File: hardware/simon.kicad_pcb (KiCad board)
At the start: 2 copper layers, 19 parts, among them SW0 SW_RED, SW1 SW_YELLOW, SW2 SW_GREEN, SW3 SW_BLUE

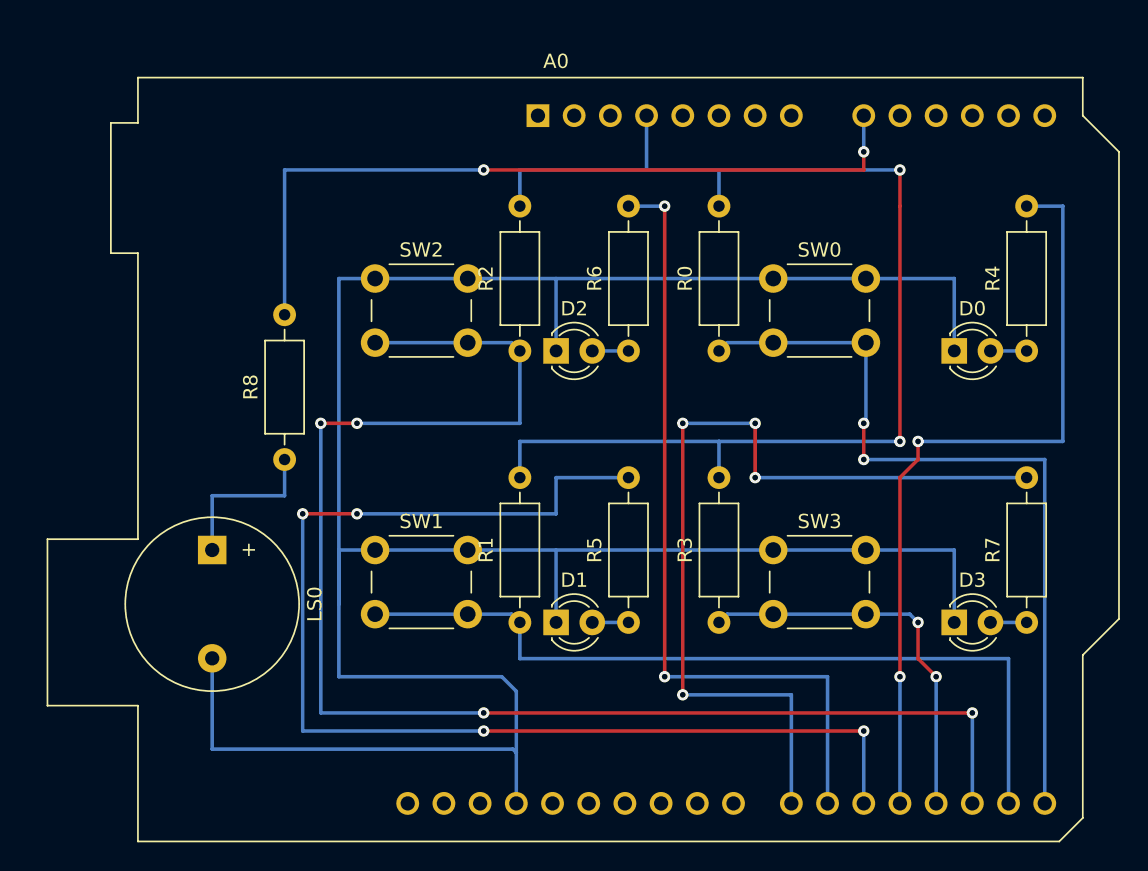
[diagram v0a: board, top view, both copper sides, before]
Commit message: hardware schematics done, test code included
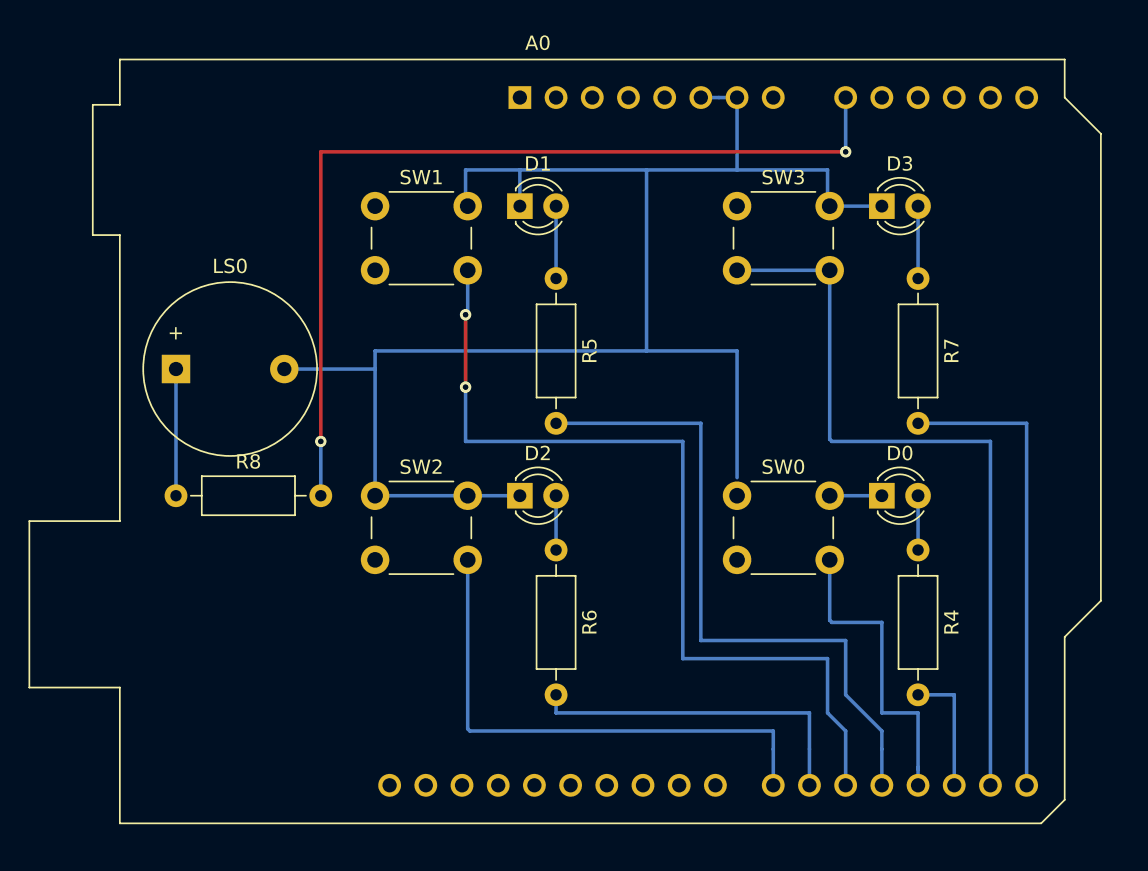
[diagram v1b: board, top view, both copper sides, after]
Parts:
- removed R0, R1, R2, R3: 1k, Resistor_THT:R_Axial_DIN0207_L6.3mm_D2.5mm_P10.16mm_Horizontal
- R8: value ??? -> 110
- moved D3 29.6 mm to (67.3, 24.1)
- moved D1 29.3 mm to (41.9, 24.1)
- moved R7 25.3 mm to (69.8, 29.2), turned to 270 degrees
- moved R5 24.7 mm to (44.5, 29.2), turned to 270 degrees
- moved SW3 24.3 mm to (57.1, 24.1)
- moved SW1 24.1 mm to (31.8, 24.1)
- moved R4 15.9 mm to (69.8, 48.3), turned to 270 degrees
- moved SW0 15.5 mm to (57.1, 44.5)
- moved SW2 15.2 mm to (31.8, 44.5)
- moved R6 14.9 mm to (44.5, 48.3), turned to 270 degrees
- moved LS0 13.0 mm to (17.8, 35.6), turned to 0 degrees
- moved D0 11.4 mm to (67.3, 44.5)
- moved D2 10.5 mm to (41.9, 44.5)
- moved R8 8.03 mm to (17.8, 44.5), turned to 0 degrees
- moved A0 1.80 mm to (41.9, 16.5)
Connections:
- net ARD_A0 renamed BUZZ
- net ARD_D6 renamed LED_GRE
- A0 pad 15: ARD_D0 -> LED_BLU
- A0 pad 16: ARD_D1 -> SWC_BLU
- A0 pad 17: ARD_D2 -> LED_RED
- A0 pad 18: ARD_D3 -> SWC_RED
- A0 pad 19: ARD_D4 -> LED_YLW
- A0 pad 20: ARD_D5 -> SWC_YLW
- A0 pad 22: ARD_D7 -> SWC_GRE
- R4 pad 2: ARD_D4 -> LED_RED
- R5 pad 2: ARD_D5 -> LED_YLW
- R7 pad 2: ARD_D7 -> LED_BLU
- SW0 pad 2: ARD_D0 -> SWC_RED
- SW1 pad 2: ARD_D1 -> SWC_YLW
- SW2 pad 2: ARD_D2 -> SWC_GRE
- SW3 pad 2: ARD_D3 -> SWC_BLU
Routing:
- net ARD_D2: track 101.8 -> 0.00 mm, vias 4 -> 0
- net VCC: track 86.4 -> 0.00 mm, vias 2 -> 0
- net ARD_D5: track 85.1 -> 0.00 mm, vias 4 -> 0
- net GND: track 187.0 -> 121.8 mm
- net ARD_D7: track 62.2 -> 0.00 mm, vias 4 -> 0
- net SWC_YLW: track 0.00 -> 62.1 mm, vias 0 -> 2
- net ARD_D1: track 57.4 -> 0.00 mm
- net ARD_D0: track 55.6 -> 0.00 mm, vias 2 -> 0
- net ARD_D4: track 55.1 -> 0.00 mm, vias 2 -> 0
- net SWC_BLU: track 0.00 -> 53.8 mm
- net LED_YLW: track 0.00 -> 46.8 mm
- net SWC_GRE: track 0.00 -> 37.2 mm
- net LED_BLU: track 0.00 -> 33.0 mm
- net LED_GRE: track 55.9 -> 24.1 mm, vias 2 -> 0
- net ARD_D3: track 27.7 -> 0.00 mm, vias 2 -> 0
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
